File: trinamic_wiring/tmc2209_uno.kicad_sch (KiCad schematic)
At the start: 3 parts, among them M1 Stepper_Motor_QSH2818-32-07-0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

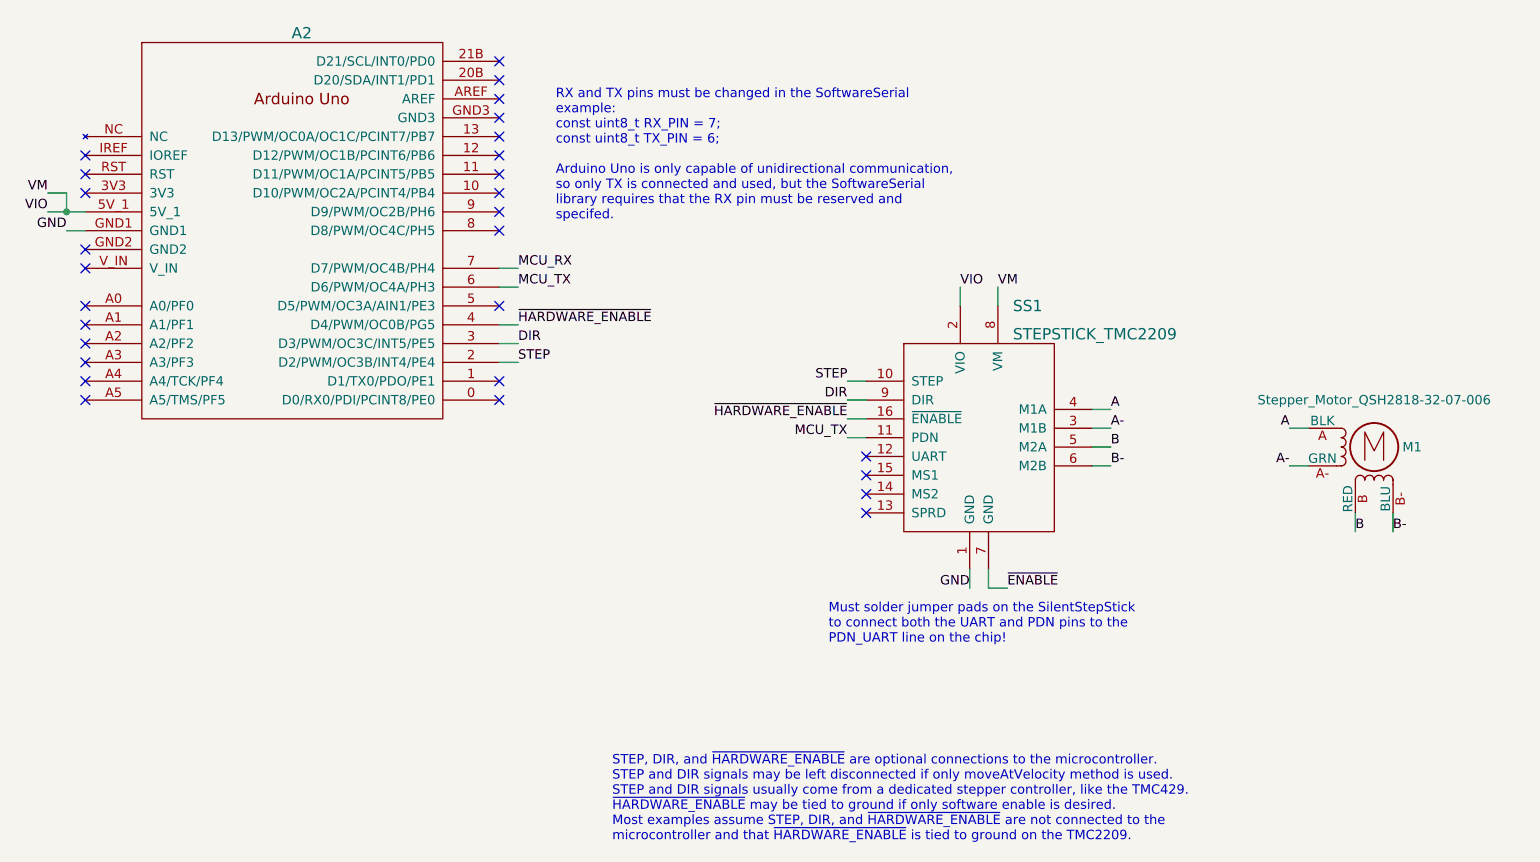
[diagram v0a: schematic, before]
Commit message: Adjust large schematics for ease of reading
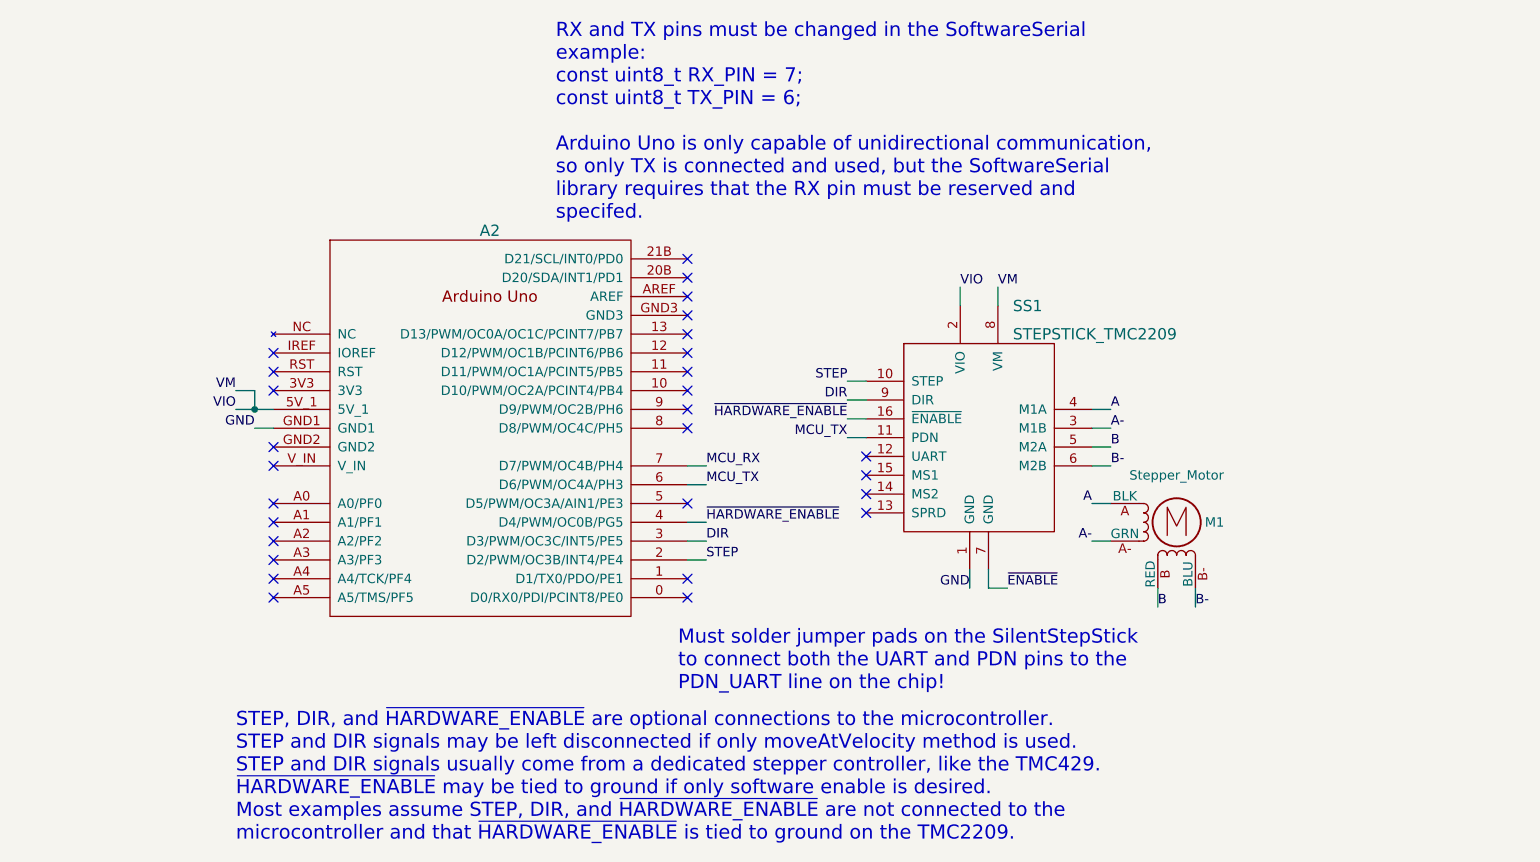
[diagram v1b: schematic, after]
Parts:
- M1: value Stepper_Motor_QSH2818-32-07-006 -> Stepper_Motor
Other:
- moved on the sheet: A2, M1
